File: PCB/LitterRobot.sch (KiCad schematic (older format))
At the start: 6 parts, among them J1 DF11C-4DP-2V(57), J2 DF11C-6DP-2V(57), J3 DF11C-8DP-2V(57), J4 DF11C-6DP-2V(57)

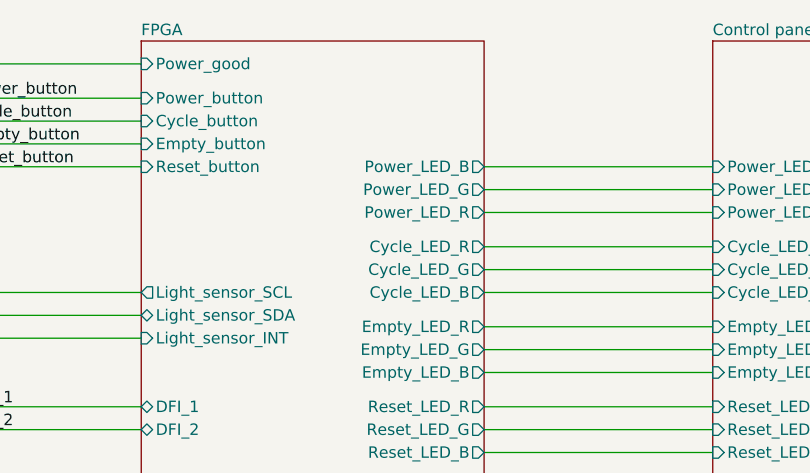
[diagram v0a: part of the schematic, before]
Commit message: Complete routing all signals
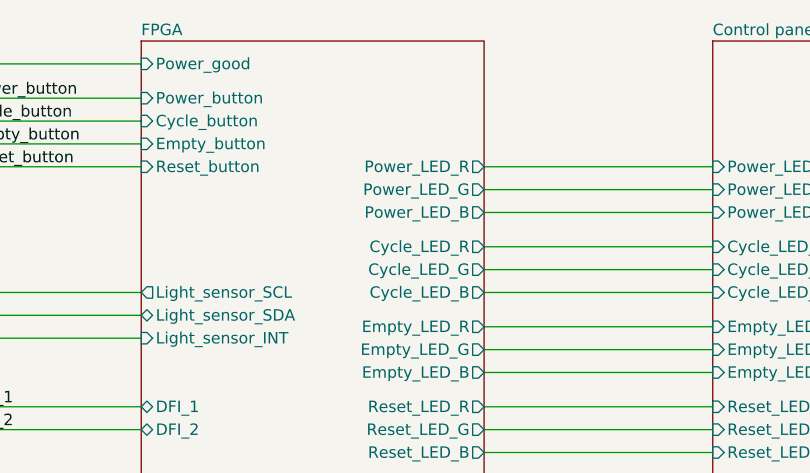
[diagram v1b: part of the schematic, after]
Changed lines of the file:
@@
 F25 "Right_LED_B" O R 8000 3850 50
 F26 "Power_button" I L 6500 1250 50
-F27 "Power_LED_B" O R 8000 1550 50
+F27 "Power_LED_B" O R 8000 1750 50
 F28 "Power_LED_G" O R 8000 1650 50
-F29 "Power_LED_R" O R 8000 1750 50
+F29 "Power_LED_R" O R 8000 1550 50
 F30 "Dome_LED" O R 8000 5600 50
 F31 "Light_sensor_SDA" B L 6500 2200 50
